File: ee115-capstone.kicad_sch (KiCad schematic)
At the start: 24 parts, among them J2 9V_BATTERY, J4 Conn_01x04_Pin, J5 Conn_01x03_Pin, Q1 PMOS, Q2 NMOS, SW3 SW_Push, SW4 GF-123-0054, U13 LD39150DT33-R

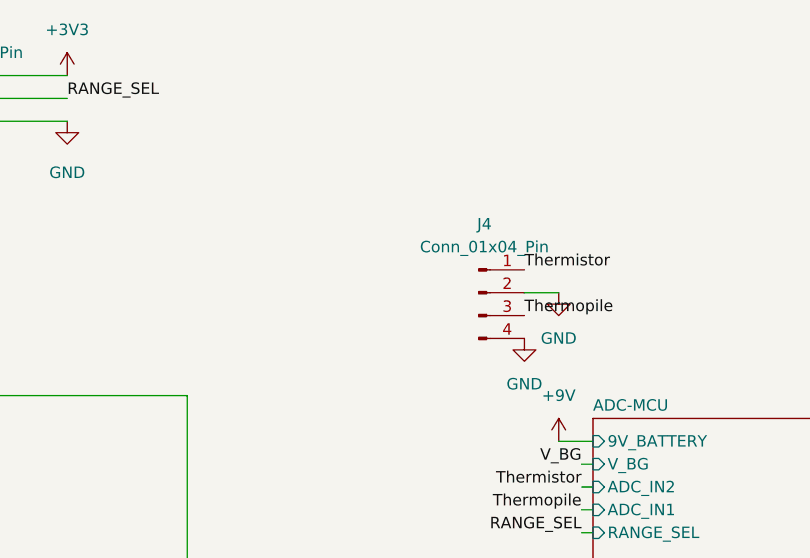
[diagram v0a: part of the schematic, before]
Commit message: Revert "init pcb"
This reverts commit 9bdb2c35d816e1c0bde8256efe77796e7b93f096.
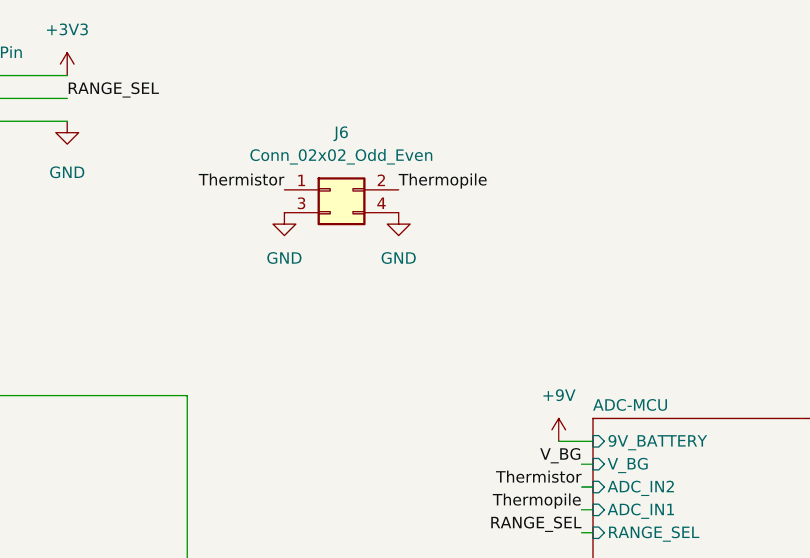
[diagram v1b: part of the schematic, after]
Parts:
- removed J4: Conn_01x04_Pin, Connector_Molex:Molex_KK-254_AE-6410-04A_1x04_P2.54mm_Vertical, symbol Connector:Conn_01x04_Pin
- added J6: Conn_02x02_Odd_Even, Connector_Molex:Molex_Mega-Fit_76829-0004_2x02_P5.70mm_Vertical, symbol Connector_Generic:Conn_02x02_Odd_Even
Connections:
- net GND: now also J6.3 (Pin_3), J6.4 (Pin_4)
- net Thermistor: now also J6.1 (Pin_1)
- net Thermopile: now also J6.2 (Pin_2)
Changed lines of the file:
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@@
-	(wire
-		(pts
-			(xy 185.42 45.72) (xy 189.23 45.72)
-		)
-		(stroke
-			(width 0)
-			(type default)
-		)
-	)
 	(wire
 		(pts
@@
 		)
 	)
-	(label "Thermopile"
-		(at 185.42 48.26 0)
-		(effects
-			(font
-				(size 1.27 1.27)
-			)
-			(justify left bottom)
-		)
-	)
 	(label "V_BG"
 		(at 191.77 64.77 180)
@@
 		)
 	)
+	(label "Thermistor"
+		(at 158.75 34.29 180)
+		(effects
+			(font
+				(size 1.27 1.27)
+			)
+			(justify right bottom)
+		)
+	)
 	(label "Thermopile"
 		(at 189.23 107.95 180)
@@
 		)
 	)
+	(label "Thermopile"
+		(at 171.45 34.29 0)
+		(effects
+			(font
+				(size 1.27 1.27)
+			)
+			(justify left bottom)
+		)
+	)
 	(label "POWER_LATCH"
 		(at 71.12 95.25 0)
@@
 		)
 	)
-	(label "Thermistor"
-		(at 185.42 43.18 0)
-		(effects
-			(font
-				(size 1.27 1.27)
-			)
-			(justify left bottom)
-		)
-	)
 	(label "Thermopile"
 		(at 191.77 69.85 180)
@@
 	)
 	(symbol
+		(lib_id "Connector_Generic:Conn_02x02_Odd_Even")
+		(at 163.83 34.29 0)
+		(unit 1)
+		(exclude_from_sim no)
+		(in_bom yes)
+		(on_board yes)
+		(dnp no)
+		(fields_autoplaced yes)
+		(property "Reference" "J6"
+			(at 165.1 27.94 0)
+			(effects
+				(font
+					(size 1.27 1.27)
+				)
+			)
+		)
+		(property "Value" "Conn_02x02_Odd_Even"
+			(at 165.1 30.48 0)
+			(effects
+				(font
+					(size 1.27 1.27)
+				)
+			)
+		)
+		(property "Footprint" "Connector_Molex:Molex_Mega-Fit_76829-0004_2x02_P5.70mm_Vertical"
+			(at 163.83 34.29 0)
+			(effects
+				(font
+					(size 1.27 1.27)
+				)
+				(hide yes)
+			)
+		)
+		(property "Datasheet" "~"
+			(at 163.83 34.29 0)
+			(effects
+				(font
+					(size 1.27 1.27)
+				)
+				(hide yes)
+			)
+		)
+		(property "Description" "Generic connector, double row, 02x02, odd/even pin numbering scheme (row 1 odd numbers, row 2 even numbers), script generated (kicad-library-utils/schlib/autogen/connector/)"
+			(at 163.83 34.29 0)
+			(effects
+				(font
+					(size 1.27 1.27)
+				)
+				(hide yes)
+			)
+		)
+		(pin "1"
+		)
+		(pin "4"
+		)
+		(pin "2"
+		)
+		(pin "3"
+		)
+		(instances
+			(project ""
+				(path "/80dfed98-7d85-4c9a-bb85-182165e7352f"
+					(reference "J6")
+					(unit 1)
+				)
+			)
+		)
+	)
+	(symbol
 		(lib_id "Connector:TestPoint")
 		(at 33.655 82.55 0)
@@
 	)
 	(symbol
-		(lib_id "power:GND")
-		(at 189.23 45.72 0)
-		(unit 1)
-		(exclude_from_sim no)
-		(in_bom yes)
-		(on_board yes)
-		(dnp no)
-		(fields_autoplaced yes)
-		(property "Reference" "#PWR0122"
-			(at 189.23 52.07 0)
-			(effects
-				(font
-					(size 1.27 1.27)
-				)
-				(hide yes)
-			)
-		)
-		(property "Value" "GND"
-			(at 189.23 50.8 0)
-			(effects
-				(font
-					(size 1.27 1.27)
-				)
-			)
-		)
-		(property "Footprint" ""
-			(at 189.23 45.72 0)
-			(effects
-				(font
-					(size 1.27 1.27)
-				)
-				(hide yes)
-			)
-		)
-		(property "Datasheet" ""
-			(at 189.23 45.72 0)
-			(effects
-				(font
-					(size 1.27 1.27)
-				)
-				(hide yes)
-			)
-		)
-		(property "Description" "Power symbol creates a global label with name \"GND\" , ground"
-			(at 189.23 45.72 0)
-			(effects
-				(font
-					(size 1.27 1.27)
-				)
-				(hide yes)
-			)
-		)
-		(pin "1"
-		)
-		(instances
-			(project "ee115-capstone"
-				(path "/80dfed98-7d85-4c9a-bb85-182165e7352f"
-					(reference "#PWR0122")
-					(unit 1)
-				)
-			)
-		)
-	)
-	(symbol
 		(lib_id "Device:C")
 		(at 90.17 60.96 0)
@@
 				(path "/80dfed98-7d85-4c9a-bb85-182165e7352f"
 					(reference "#PWR0120")
+					(unit 1)
+				)
+			)
+		)
+	)
+	(symbol
+		(lib_id "power:GND")
+		(at 158.75 36.83 0)
+		(unit 1)
+		(exclude_from_sim no)
+		(in_bom yes)
+		(on_board yes)
+		(dnp no)
+		(fields_autoplaced yes)
+		(property "Reference" "#PWR0104"
+			(at 158.75 43.18 0)
+			(effects
+				(font
+					(size 1.27 1.27)
+				)
+				(hide yes)
+			)
+		)
+		(property "Value" "GND"
+			(at 158.75 41.91 0)
+			(effects
+				(font
+					(size 1.27 1.27)
+				)
+			)
+		)
+		(property "Footprint" ""
+			(at 158.75 36.83 0)
+			(effects
+				(font
+					(size 1.27 1.27)
+				)
+				(hide yes)
+			)
+		)
+		(property "Datasheet" ""
+			(at 158.75 36.83 0)
+			(effects
+				(font
+					(size 1.27 1.27)
+				)
+				(hide yes)
+			)
+		)
+		(property "Description" "Power symbol creates a global label with name \"GND\" , ground"
+			(at 158.75 36.83 0)
+			(effects
+				(font
+					(size 1.27 1.27)
+				)
+				(hide yes)
+			)
+		)
+		(pin "1"
+		)
+		(instances
+			(project "ee115-capstone"
+				(path "/80dfed98-7d85-4c9a-bb85-182165e7352f"
+					(reference "#PWR0104")
 					(unit 1)
 				)
@@
 	(symbol
 		(lib_id "power:GND")
-		(at 185.42 50.8 0)
+		(at 171.45 36.83 0)
 		(unit 1)
 		(exclude_from_sim no)
@@
 		(fields_autoplaced yes)
 		(property "Reference" "#PWR0103"
-			(at 185.42 57.15 0)
+			(at 171.45 43.18 0)
 			(effects
 				(font
@@
 		)
 		(property "Value" "GND"
-			(at 185.42 55.88 0)
+			(at 171.45 41.91 0)
 			(effects
 				(font
@@
 		)
 		(property "Footprint" ""
-			(at 185.42 50.8 0)
+			(at 171.45 36.83 0)
 			(effects
 				(font
@@
 		)
 		(property "Datasheet" ""
-			(at 185.42 50.8 0)
+			(at 171.45 36.83 0)
 			(effects
 				(font
@@
 		)
 		(property "Description" "Power symbol creates a global label with name \"GND\" , ground"
-			(at 185.42 50.8 0)
+			(at 171.45 36.83 0)
 			(effects
 				(font
@@
 					(unit 1)
 				)
-			)
-		)
-	)
-	(symbol
-		(lib_id "Connector:Conn_01x04_Pin")
-		(at 180.34 45.72 0)
-		(unit 1)
-		(exclude_from_sim no)
-		(in_bom yes)
-		(on_board yes)
-		(dnp no)
-		(fields_autoplaced yes)
-		(property "Reference" "J4"
-			(at 180.975 38.1 0)
-			(effects
-				(font
-					(size 1.27 1.27)
-				)
-			)
-		)
-		(property "Value" "Conn_01x04_Pin"
-			(at 180.975 40.64 0)
-			(effects
-				(font
-					(size 1.27 1.27)
-				)
-			)
-		)
-		(property "Footprint" "Connector_Molex:Molex_KK-254_AE-6410-04A_1x04_P2.54mm_Vertical"
-			(at 180.34 45.72 0)
-			(effects
-				(font
-					(size 1.27 1.27)
-				)
-				(hide yes)
-			)
-		)
-		(property "Datasheet" "~"
-			(at 180.34 45.72 0)
-			(effects
-				(font
-					(size 1.27 1.27)
-				)
-				(hide yes)
-			)
-		)
-		(property "Description" "Generic connector, single row, 01x04, script generated"
-			(at 180.34 45.72 0)
-			(effects
-				(font
-					(size 1.27 1.27)
-				)
-				(hide yes)
-			)
-		)
-		(pin "1"
-		)
-		(pin "2"
-		)
-		(pin "3"
-		)
-		(pin "4"
-		)
-		(instances
-			(project ""
-				(path "/80dfed98-7d85-4c9a-bb85-182165e7352f"
-					(reference "J4")
-					(unit 1)
-				)

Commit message: init pcb
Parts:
- removed J6: Conn_02x02_Odd_Even, Connector_Molex:Molex_Mega-Fit_76829-0004_2x02_P5.70mm_Vertical, symbol Connector_Generic:Conn_02x02_Odd_Even
- added J4: Conn_01x04_Pin, Connector_Molex:Molex_KK-254_AE-6410-04A_1x04_P2.54mm_Vertical, symbol Connector:Conn_01x04_Pin
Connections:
- net GND: now also J4.2 (Pin_2), J4.4 (Pin_4)
- net Thermistor: now also J4.1 (Pin_1)
- net Thermopile: now also J4.3 (Pin_3)
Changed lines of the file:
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@@
+	(wire
+		(pts
+			(xy 185.42 45.72) (xy 189.23 45.72)
+		)
+		(stroke
+			(width 0)
+			(type default)
+		)
+	)
 	(wire
 		(pts
@@
 		)
 	)
+	(label "Thermopile"
+		(at 185.42 48.26 0)
+		(effects
+			(font
+				(size 1.27 1.27)
+			)
+			(justify left bottom)
+		)
+	)
 	(label "V_BG"
 		(at 191.77 64.77 180)
@@
 		)
 	)
-	(label "Thermistor"
-		(at 158.75 34.29 180)
-		(effects
-			(font
-				(size 1.27 1.27)
-			)
-			(justify right bottom)
-		)
-	)
 	(label "Thermopile"
 		(at 189.23 107.95 180)
@@
 		)
 	)
-	(label "Thermopile"
-		(at 171.45 34.29 0)
-		(effects
-			(font
-				(size 1.27 1.27)
-			)
-			(justify left bottom)
-		)
-	)
 	(label "POWER_LATCH"
 		(at 71.12 95.25 0)
@@
 		)
 	)
+	(label "Thermistor"
+		(at 185.42 43.18 0)
+		(effects
+			(font
+				(size 1.27 1.27)
+			)
+			(justify left bottom)
+		)
+	)
 	(label "Thermopile"
 		(at 191.77 69.85 180)
@@
 	)
 	(symbol
-		(lib_id "Connector_Generic:Conn_02x02_Odd_Even")
-		(at 163.83 34.29 0)
-		(unit 1)
-		(exclude_from_sim no)
-		(in_bom yes)
-		(on_board yes)
-		(dnp no)
-		(fields_autoplaced yes)
-		(property "Reference" "J6"
-			(at 165.1 27.94 0)
-			(effects
-				(font
-					(size 1.27 1.27)
-				)
-			)
-		)
-		(property "Value" "Conn_02x02_Odd_Even"
-			(at 165.1 30.48 0)
-			(effects
-				(font
-					(size 1.27 1.27)
-				)
-			)
-		)
-		(property "Footprint" "Connector_Molex:Molex_Mega-Fit_76829-0004_2x02_P5.70mm_Vertical"
-			(at 163.83 34.29 0)
-			(effects
-				(font
-					(size 1.27 1.27)
-				)
-				(hide yes)
-			)
-		)
-		(property "Datasheet" "~"
-			(at 163.83 34.29 0)
-			(effects
-				(font
-					(size 1.27 1.27)
-				)
-				(hide yes)
-			)
-		)
-		(property "Description" "Generic connector, double row, 02x02, odd/even pin numbering scheme (row 1 odd numbers, row 2 even numbers), script generated (kicad-library-utils/schlib/autogen/connector/)"
-			(at 163.83 34.29 0)
-			(effects
-				(font
-					(size 1.27 1.27)
-				)
-				(hide yes)
-			)
-		)
-		(pin "1"
-		)
-		(pin "4"
-		)
-		(pin "2"
-		)
-		(pin "3"
-		)
-		(instances
-			(project ""
-				(path "/80dfed98-7d85-4c9a-bb85-182165e7352f"
-					(reference "J6")
-					(unit 1)
-				)
-			)
-		)
-	)
-	(symbol
 		(lib_id "Connector:TestPoint")
 		(at 33.655 82.55 0)
@@
 	)
 	(symbol
+		(lib_id "power:GND")
+		(at 189.23 45.72 0)
+		(unit 1)
+		(exclude_from_sim no)
+		(in_bom yes)
+		(on_board yes)
+		(dnp no)
+		(fields_autoplaced yes)
+		(property "Reference" "#PWR0122"
+			(at 189.23 52.07 0)
+			(effects
+				(font
+					(size 1.27 1.27)
+				)
+				(hide yes)
+			)
+		)
+		(property "Value" "GND"
+			(at 189.23 50.8 0)
+			(effects
+				(font
+					(size 1.27 1.27)
+				)
+			)
+		)
+		(property "Footprint" ""
+			(at 189.23 45.72 0)
+			(effects
+				(font
+					(size 1.27 1.27)
+				)
+				(hide yes)
+			)
+		)
+		(property "Datasheet" ""
+			(at 189.23 45.72 0)
+			(effects
+				(font
+					(size 1.27 1.27)
+				)
+				(hide yes)
+			)
+		)
+		(property "Description" "Power symbol creates a global label with name \"GND\" , ground"
+			(at 189.23 45.72 0)
+			(effects
+				(font
+					(size 1.27 1.27)
+				)
+				(hide yes)
+			)
+		)
+		(pin "1"
+		)
+		(instances
+			(project "ee115-capstone"
+				(path "/80dfed98-7d85-4c9a-bb85-182165e7352f"
+					(reference "#PWR0122")
+					(unit 1)
+				)
+			)
+		)
+	)
+	(symbol
 		(lib_id "Device:C")
 		(at 90.17 60.96 0)
@@
 				(path "/80dfed98-7d85-4c9a-bb85-182165e7352f"
 					(reference "#PWR0120")
-					(unit 1)
-				)
-			)
-		)
-	)
-	(symbol
-		(lib_id "power:GND")
-		(at 158.75 36.83 0)
-		(unit 1)
-		(exclude_from_sim no)
-		(in_bom yes)
-		(on_board yes)
-		(dnp no)
-		(fields_autoplaced yes)
-		(property "Reference" "#PWR0104"
-			(at 158.75 43.18 0)
-			(effects
-				(font
-					(size 1.27 1.27)
-				)
-				(hide yes)
-			)
-		)
-		(property "Value" "GND"
-			(at 158.75 41.91 0)
-			(effects
-				(font
-					(size 1.27 1.27)
-				)
-			)
-		)
-		(property "Footprint" ""
-			(at 158.75 36.83 0)
-			(effects
-				(font
-					(size 1.27 1.27)
-				)
-				(hide yes)
-			)
-		)
-		(property "Datasheet" ""
-			(at 158.75 36.83 0)
-			(effects
-				(font
-					(size 1.27 1.27)
-				)
-				(hide yes)
-			)
-		)
-		(property "Description" "Power symbol creates a global label with name \"GND\" , ground"
-			(at 158.75 36.83 0)
-			(effects
-				(font
-					(size 1.27 1.27)
-				)
-				(hide yes)
-			)
-		)
-		(pin "1"
-		)
-		(instances
-			(project "ee115-capstone"
-				(path "/80dfed98-7d85-4c9a-bb85-182165e7352f"
-					(reference "#PWR0104")
 					(unit 1)
 				)
@@
 	(symbol
 		(lib_id "power:GND")
-		(at 171.45 36.83 0)
+		(at 185.42 50.8 0)
 		(unit 1)
 		(exclude_from_sim no)
@@
 		(fields_autoplaced yes)
 		(property "Reference" "#PWR0103"
-			(at 171.45 43.18 0)
+			(at 185.42 57.15 0)
 			(effects
 				(font
@@
 		)
 		(property "Value" "GND"
-			(at 171.45 41.91 0)
+			(at 185.42 55.88 0)
 			(effects
 				(font
@@
 		)
 		(property "Footprint" ""
-			(at 171.45 36.83 0)
+			(at 185.42 50.8 0)
 			(effects
 				(font
@@
 		)
 		(property "Datasheet" ""
-			(at 171.45 36.83 0)
+			(at 185.42 50.8 0)
 			(effects
 				(font
@@
 		)
 		(property "Description" "Power symbol creates a global label with name \"GND\" , ground"
-			(at 171.45 36.83 0)
+			(at 185.42 50.8 0)
 			(effects
 				(font
@@
 					(unit 1)
 				)
+			)
+		)
+	)
+	(symbol
+		(lib_id "Connector:Conn_01x04_Pin")
+		(at 180.34 45.72 0)
+		(unit 1)
+		(exclude_from_sim no)
+		(in_bom yes)
+		(on_board yes)
+		(dnp no)
+		(fields_autoplaced yes)
+		(property "Reference" "J4"
+			(at 180.975 38.1 0)
+			(effects
+				(font
+					(size 1.27 1.27)
+				)
+			)
+		)
+		(property "Value" "Conn_01x04_Pin"
+			(at 180.975 40.64 0)
+			(effects
+				(font
+					(size 1.27 1.27)
+				)
+			)
+		)
+		(property "Footprint" "Connector_Molex:Molex_KK-254_AE-6410-04A_1x04_P2.54mm_Vertical"
+			(at 180.34 45.72 0)
+			(effects
+				(font
+					(size 1.27 1.27)
+				)
+				(hide yes)
+			)
+		)
+		(property "Datasheet" "~"
+			(at 180.34 45.72 0)
+			(effects
+				(font
+					(size 1.27 1.27)
+				)
+				(hide yes)
+			)
+		)
+		(property "Description" "Generic connector, single row, 01x04, script generated"
+			(at 180.34 45.72 0)
+			(effects
+				(font
+					(size 1.27 1.27)
+				)
+				(hide yes)
+			)
+		)
+		(pin "1"
+		)
+		(pin "2"
+		)
+		(pin "3"
+		)
+		(pin "4"
+		)
+		(instances
+			(project ""
+				(path "/80dfed98-7d85-4c9a-bb85-182165e7352f"
+					(reference "J4")
+					(unit 1)
+				)
